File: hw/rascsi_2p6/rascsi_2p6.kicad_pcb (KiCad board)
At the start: 2 copper layers, 65 x 56 mm, 98 parts, among them IC1 SN74LS641-1DW, IC2 SN74LS641-1DW, IC3 SN74LS641-1DW, IC4 SN74LS641-1DW, J1 Raspberry_Pi_2_3, J2 DNP, J20 171826-4, J3 Conn_02x25_Odd_Even, J4 I2C Pinout, J5 DNP, J6 CONNFLY DB-25, J8 USB_B_Micro, J9 Conn_02x25_Odd_Even, X1 Mac, X2 Dogcow, X3 Mac, X4 Dogcow, X5 Dogcow, X6 Dogcow, X7 Pi, X8 Pi

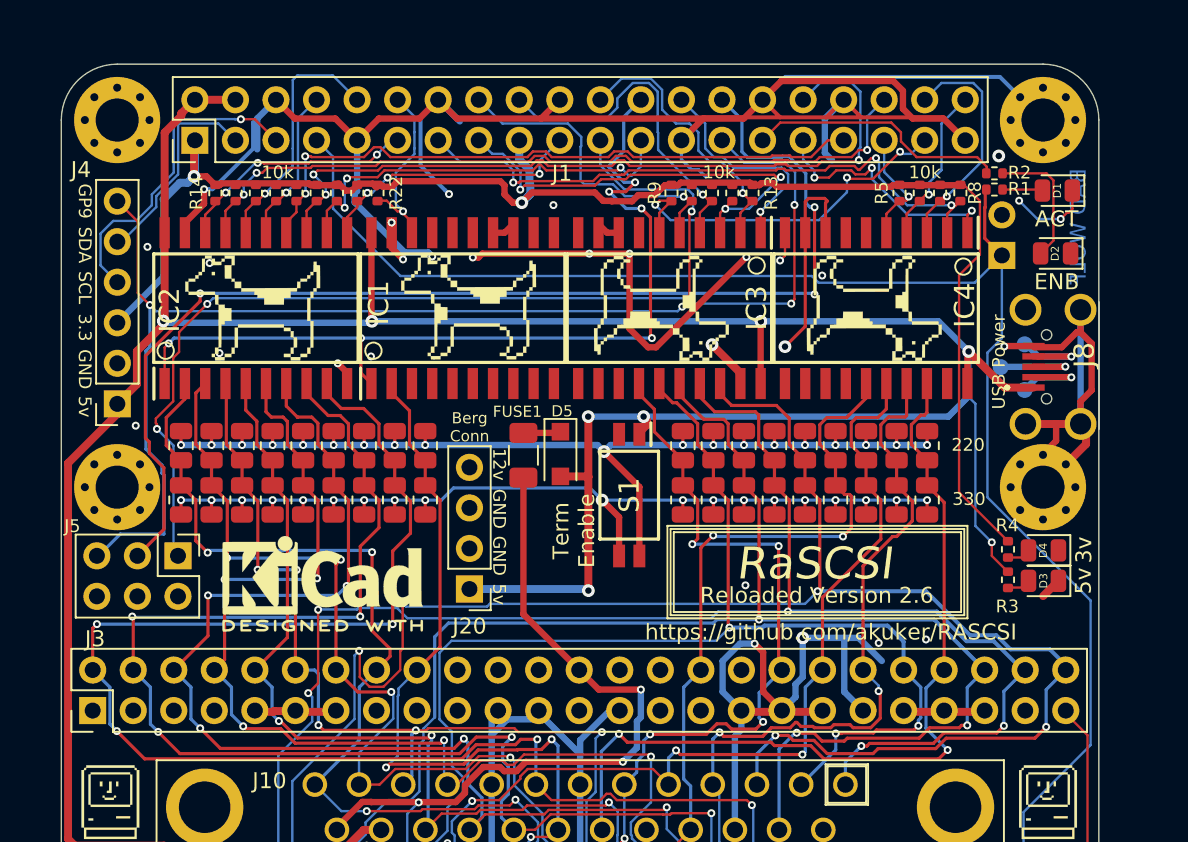
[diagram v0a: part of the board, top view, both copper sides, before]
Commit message: Updated to use 3.3v vcc instead of 5v
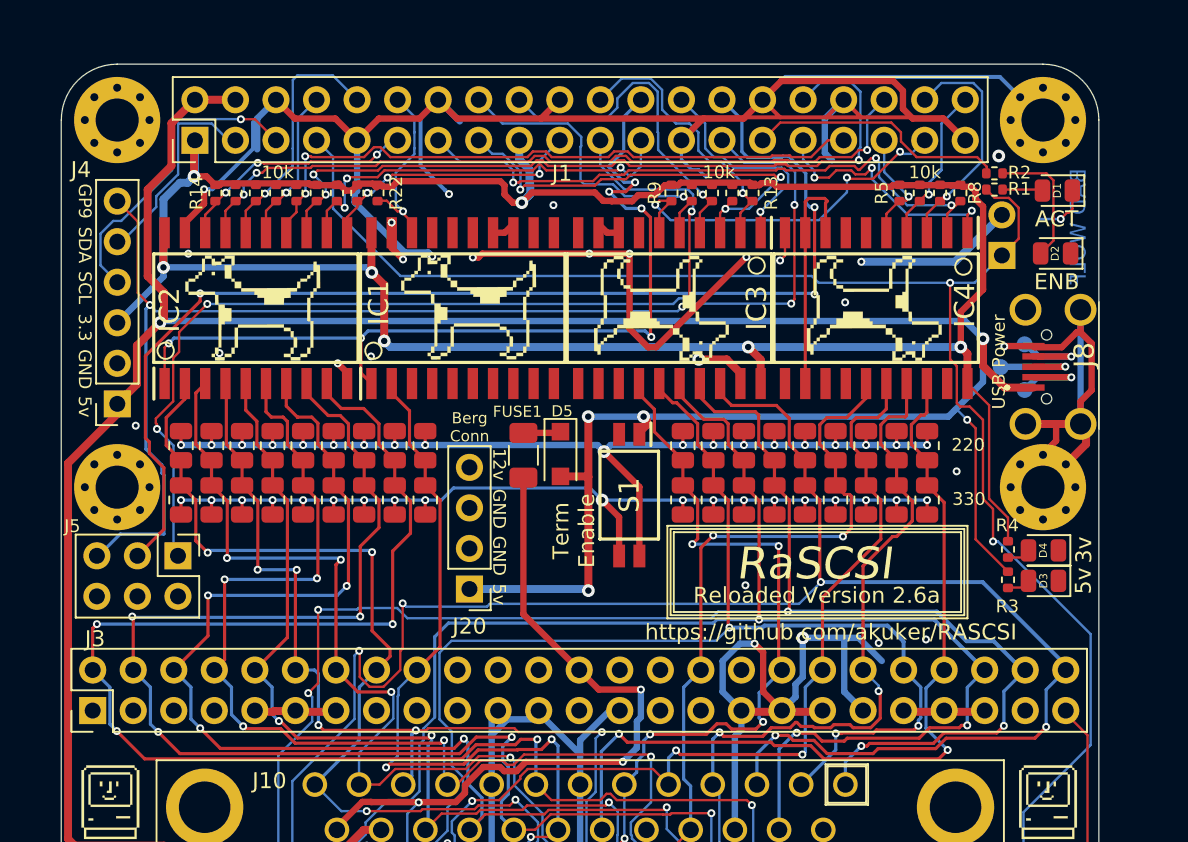
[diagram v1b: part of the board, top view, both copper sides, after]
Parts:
- removed the REF** at (190.9, 75.0)
- added REF**: KiCad-Logo_5mm_SilkScreen, Symbol:KiCad-Logo_5mm_SilkScreen, B.Cu at (191.8, 72.1)
- IC1, IC2, IC3, IC4: value SN74LS641-1DW -> SN74F245DWR
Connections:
- IC1 pad 20: +5V -> +3V3
- IC2 pad 20: +5V -> +3V3
- IC3 pad 20: +5V -> +3V3
- IC4 pad 20: +5V -> +3V3
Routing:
- net +3V3: track 96.1 -> 158.3 mm, vias 2 -> 7
- net GND: track 418.9 -> 427.8 mm, vias 29 -> 28
- net +5V: track 233.5 -> 224.7 mm, vias 8 -> 6
- net PI-ACT: track 108.0 -> 108.9 mm, vias 0 -> 2
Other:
- board text added: "Reloaded Version 2.6a"
- board text removed: "Reloaded Version 2.6"
